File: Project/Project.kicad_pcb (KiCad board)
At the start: 2 copper layers, 46 parts, among them J1 Conn_01x05_Male, J2 USB_OTG, J3 Conn_01x09_Male, J4 Conn_01x03_Female, J5 Conn_Coaxial, SW1 SW_Push, SW2 SW_Push, SW3 SW_Push, U1 CMWX1ZZABZ-078, U2 LM1117ADJ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

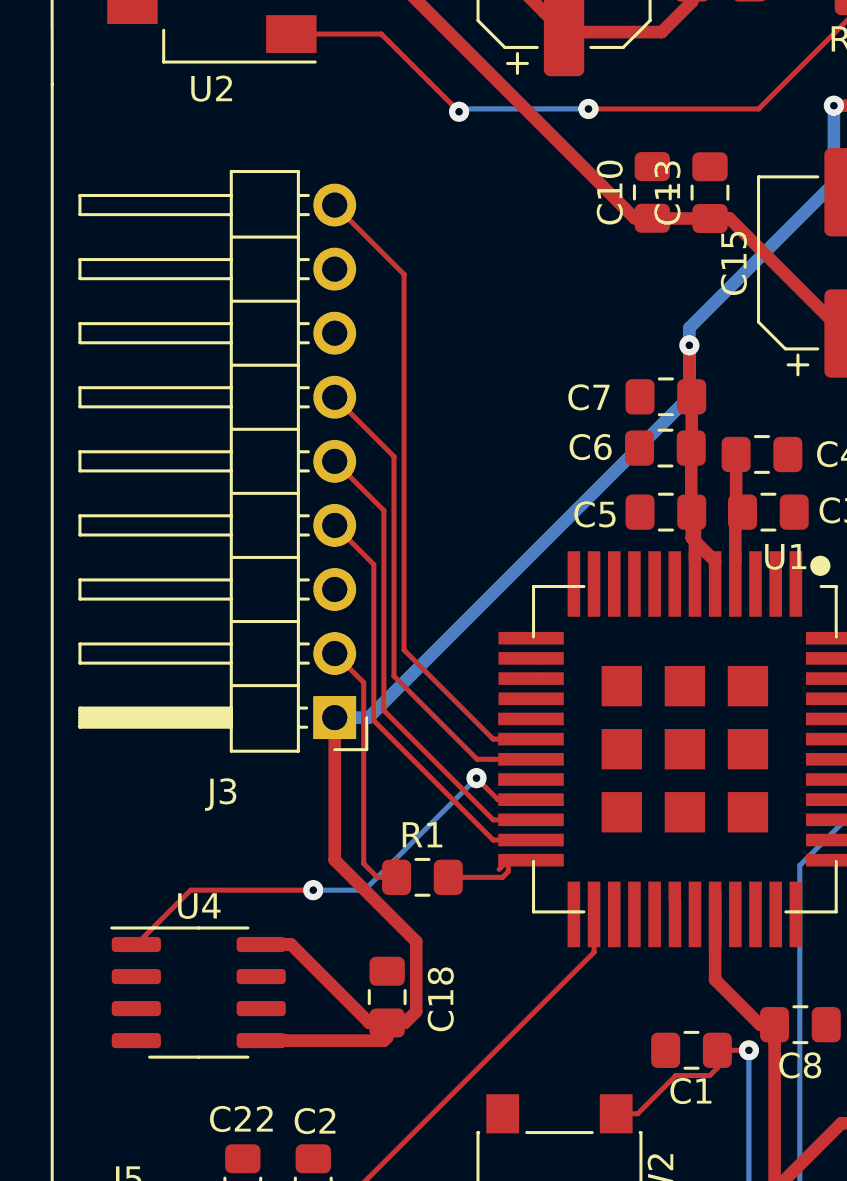
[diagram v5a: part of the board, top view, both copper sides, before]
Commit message: changed some fottprints that where wrong
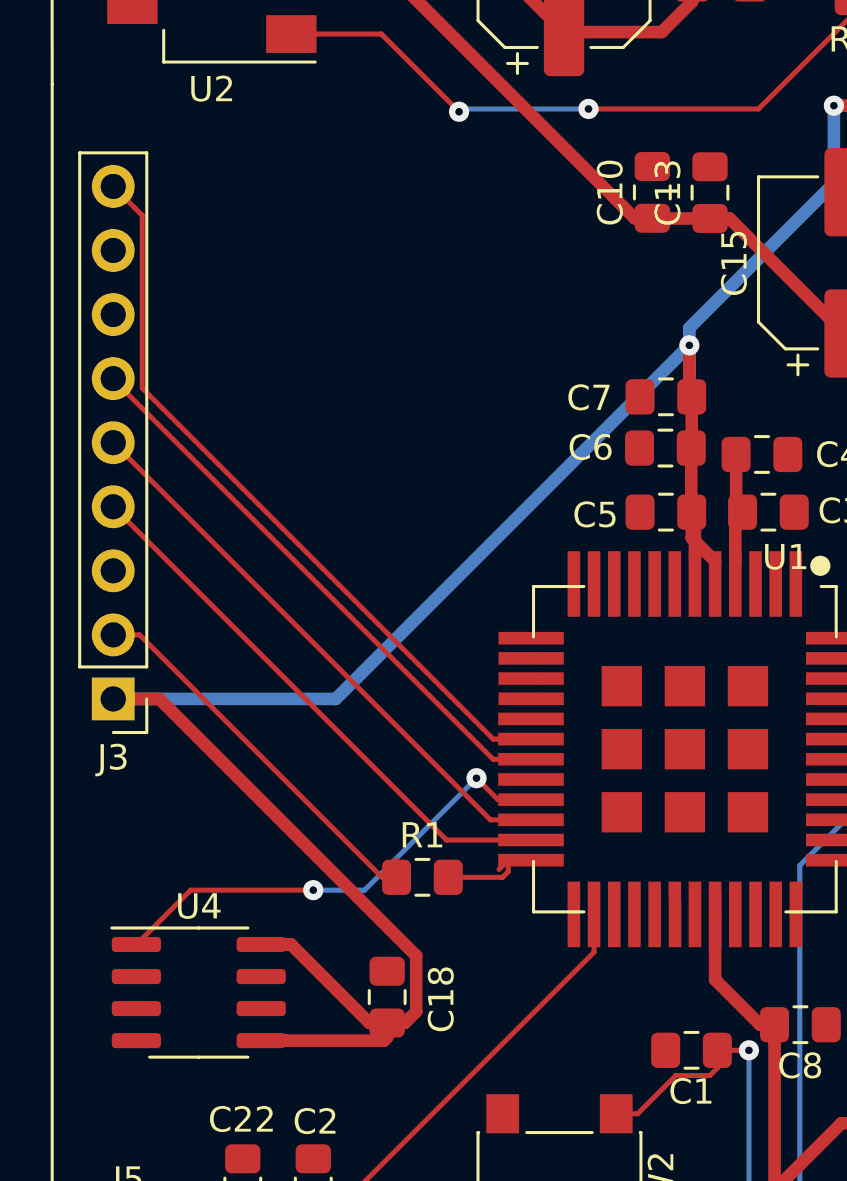
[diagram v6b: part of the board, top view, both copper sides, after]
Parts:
- J3: footprint Connector_PinHeader_2.54mm:PinHeader_1x09_P2.54mm_Horizontal -> Connector_PinHeader_2.54mm:PinHeader_1x09_P2.54mm_Vertical
- moved J3 8.81 mm to (252.4, 274.4)
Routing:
- net +3V3: track 181.7 -> 196.5 mm
- net /enable: track 11.0 -> 15.9 mm
- net /3DF(3D-FiX_indicator): track 16.6 -> 21.1 mm
- net /TX: track 18.3 -> 22.6 mm
- net /1pps(1_pulse_per_second): track 25.7 -> 29.8 mm
- net /RX: track 18.1 -> 22.1 mm

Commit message: final design??
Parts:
- removed R3: 330, Resistor_SMD:R_0805_2012Metric_Pad1.15x1.40mm_HandSolder
- removed R4: 560, Resistor_SMD:R_0805_2012Metric_Pad1.15x1.40mm_HandSolder
- added C23: 10n, Capacitor_SMD:C_0805_2012Metric_Pad1.15x1.40mm_HandSolder, F.Cu at (259.8, 245.3)
- U2: value LM1117ADJ -> SPX3819M5-L-3-3; footprint Package_TO_SOT_SMD:SOT-223 -> Package_TO_SOT_SMD:SOT-23-5
- moved C9 3.63 mm to (280.0, 245.1), turned to 90 degrees
- moved C21 3.57 mm to (260.4, 293.7)
- moved C2 3.30 mm to (263.5, 294.6), turned to 90 degrees
- moved J5 3.11 mm to (252.9, 293.8), turned to 90 degrees
- moved C22 1.09 mm to (257.5, 294.7), turned to 90 degrees
- moved U2 0.87 mm to (255.6, 245.3), turned to 90 degrees
- turned C11 to 270 degrees
- turned C12 to 270 degrees
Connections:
- C11 pad 1: +3V3 -> GND
- C11 pad 2: GND -> +3V3
- C12 pad 1: +3V3 -> GND
- C12 pad 2: GND -> +3V3
- U2 pad 1: Net-(R3-Pad2) -> Net-(C10-Pad1)
- U2 pad 2: +3V3 -> GND
- U2 pad 4: +3V3 -> Net-(C23-Pad2)
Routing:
- net Net-(R3-Pad2): track 28.0 -> 0.00 mm, vias 2 -> 0
- net Net-(C10-Pad1): track 67.6 -> 83.9 mm
- net GND: track 3.99 -> 19.3 mm, vias 1 -> 5
- net +3V3: track 196.5 -> 193.2 mm
- net Net-(C23-Pad2): track 0.00 -> 3.09 mm
- net Net-(C21-Pad2): track 7.57 -> 5.07 mm
- net Net-(R2-Pad1): track 0.00 -> 1.79 mm
- net Net-(C2-Pad2): track 19.4 -> 17.7 mm
- net (no net): vias 0 -> 3
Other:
- net class Default: trace_width 0.2 -> 0.25; via_drill 0.3 -> 0.4

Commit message: final design probably
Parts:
- C18: value 4.7u -> 0.1u
- C3, C5: value 100n -> 10u
- C4: value 100n -> 0.1n
- C6, C8: value 100n -> 1u
- C7: value 100n -> 0.1
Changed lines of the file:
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@@
       (effects (font (size 1 1) (thickness 0.15)))
     )
-    (fp_text value 100n (at 0 1.65) (layer F.Fab)
+    (fp_text value 10u (at 0 1.65) (layer F.Fab)
       (effects (font (size 1 1) (thickness 0.15)))
     )
@@
       (effects (font (size 1 1) (thickness 0.15)))
     )
-    (fp_text value 100n (at 0 1.65) (layer F.Fab)
+    (fp_text value 0.1n (at 0 1.65) (layer F.Fab)
       (effects (font (size 1 1) (thickness 0.15)))
     )
@@
       (effects (font (size 1 1) (thickness 0.15)))
     )
-    (fp_text value 100n (at 0 1.65) (layer F.Fab)
+    (fp_text value 10u (at 0 1.65) (layer F.Fab)
       (effects (font (size 1 1) (thickness 0.15)))
     )
@@
       (effects (font (size 1 1) (thickness 0.15)))
     )
-    (fp_text value 100n (at 0 1.65) (layer F.Fab)
+    (fp_text value 1u (at 0 1.65) (layer F.Fab)
       (effects (font (size 1 1) (thickness 0.15)))
     )
@@
       (effects (font (size 1 1) (thickness 0.15)))
     )
-    (fp_text value 100n (at 0 1.65) (layer F.Fab)
+    (fp_text value 0.1 (at 0 1.65) (layer F.Fab)
       (effects (font (size 1 1) (thickness 0.15)))
     )
@@
       (effects (font (size 1 1) (thickness 0.15)))
     )
-    (fp_text value 100n (at 0 1.65) (layer F.Fab)
+    (fp_text value 1u (at 0 1.65) (layer F.Fab)
       (effects (font (size 1 1) (thickness 0.15)))
     )
@@
       (effects (font (size 1 1) (thickness 0.15)))
     )
-    (fp_text value 4.7u (at 0 1.65 90) (layer F.Fab)
+    (fp_text value 0.1u (at 0 1.65 90) (layer F.Fab)
       (effects (font (size 1 1) (thickness 0.15)))
     )
@@
   (segment (start 280.282 275.152) (end 279.382 275.152) (width 0.5) (layer F.Cu) (net 30))
   (segment (start 282.082 275.152) (end 280.282 275.152) (width 0.5) (layer F.Cu) (net 30))
+  (segment (start 257.345 295.426) (end 257.556 295.215) (width 0.2) (layer F.Cu) (net 30))
   (segment (start 271.482 283.602) (end 271.482 282.902) (width 0.2) (layer F.Cu) (net 31))
-  (segment (start 257.345 295.426) (end 257.556 295.215) (width 0.2) (layer F.Cu) (net 30))
   (segment (start 263.49 293.164998) (end 263.49 293.61) (width 0.25) (layer F.Cu) (net 31))
   (segment (start 271.482 285.172998) (end 263.49 293.164998) (width 0.5) (layer F.Cu) (net 31))
